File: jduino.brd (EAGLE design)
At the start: 58.1 x 66 mm, 20 parts, among them IC1 L4931, IC2 ATMEGA48/88/168-PU, J1 Analog I/O, J2 Digital I/O, J3 Digital I/O, J5 Power Jumpers, J6 FTDI Jumpers, J7 POWER 6 - 36V, Q1 16 mHz

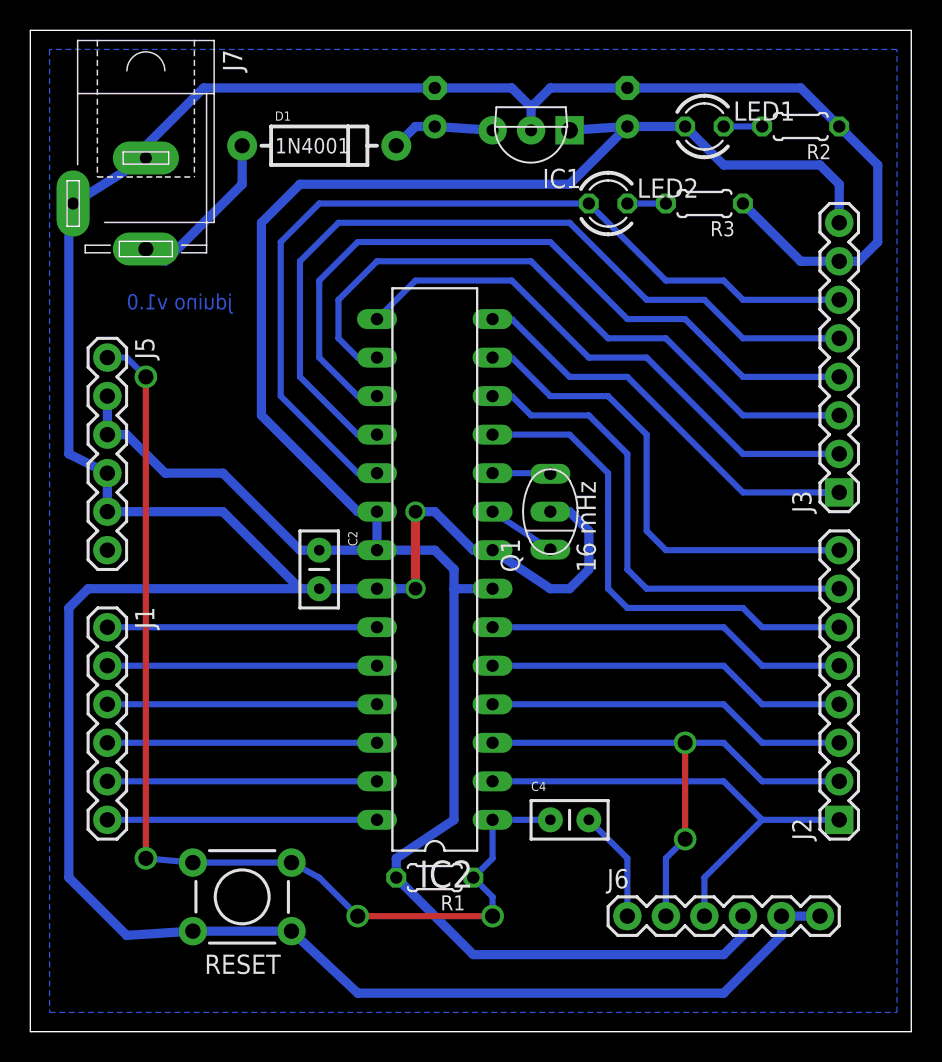
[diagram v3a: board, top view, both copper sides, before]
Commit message: Fixed pad sizes.
Replaced original parts from the Arduino robotics book with components
from the SparkFun libraries so that pads would be properly sized.
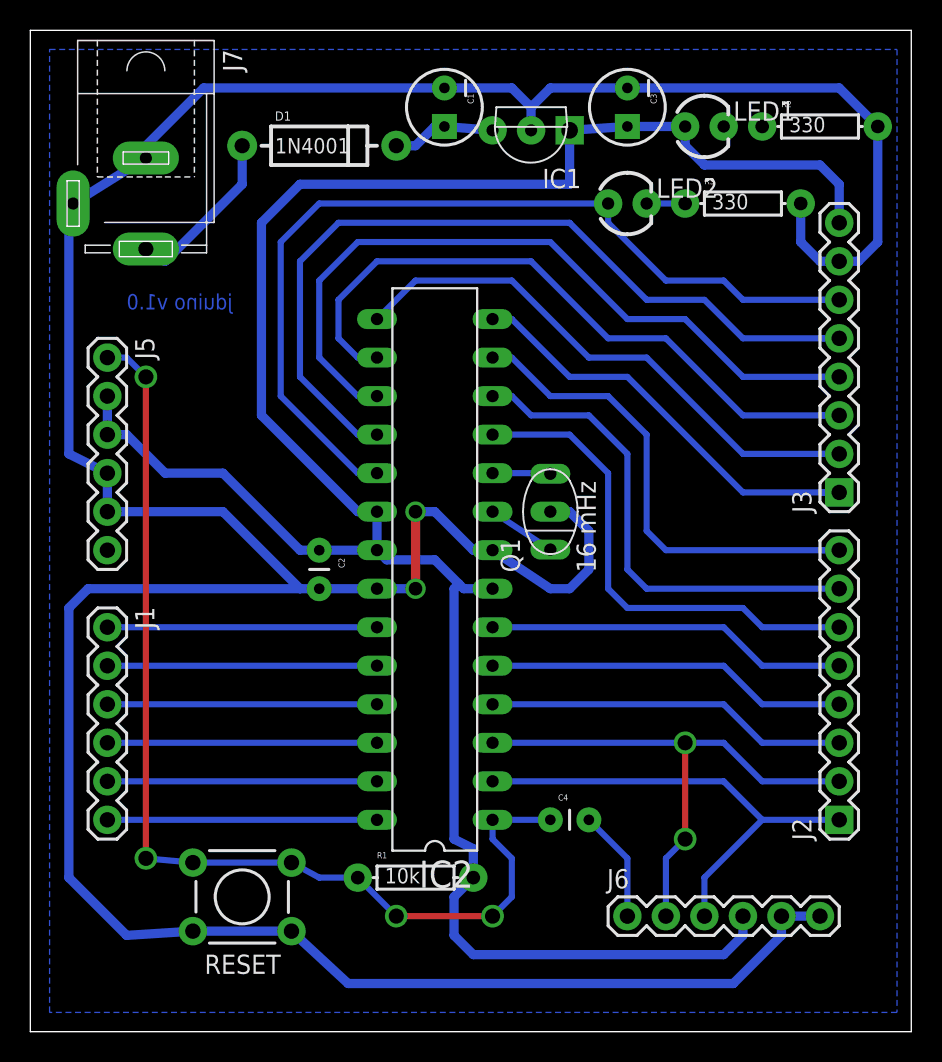
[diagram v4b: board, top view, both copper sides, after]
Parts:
- C1: value 220uf 10v -> 220 uF; device rcl:E2,5-6 -> SparkFun-Capacitors:CPOL-RADIAL-10UF-25V
- C2, C4: value 0.1uF -> 0.1 uF; device SparkFun-Passives:CAP-PTH-SMALL2 -> SparkFun-Capacitors:CAP-PTH-SMALL
- C3: value 220uf 50v -> 220 uF; device rcl:E2,5-6 -> SparkFun-Capacitors:CPOL-RADIAL-10UF-25V
- LED1: value Power LED -> POWER; device led:LED3MM -> SparkFun-LED:LED3MM
- LED2: value LED 13 -> PIN 13; device led:LED3MM -> SparkFun-LED:LED3MM
- R1: value 10K -> 10k; device rcl:0204/5 -> SparkFun-Passives:AXIAL-0.3
- R2, R3: device rcl:0204/5 -> SparkFun-Resistors:AXIAL-0.3
- moved C3 12.7 mm to (39.4, 61.0), flipped to the top, turned to 270 degrees
- moved C1 12.1 mm to (27.3, 61.0), flipped to the top, turned to 270 degrees
- moved R3 2.54 mm to (47.0, 54.6), turned to 0 degrees
- moved R1 1.27 mm to (25.4, 10.2), turned to 0 degrees
- moved R2 1.27 mm to (52.1, 59.7), turned to 0 degrees
- moved LED2 1.27 mm to (39.4, 54.6)
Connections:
- net +5V: now also C3.1, R1.P$2; no longer C1.+, R1.2
- net GND: now also C1.2, C3.2, R2.P$2, R3.P$2; no longer C1.-, C3.-, R2.1, R3.1
- net N$26: now also R2.P$1; no longer R2.2
- net N$4: now also R3.P$1; no longer R3.2
- net N$6: now also C1.1; no longer C3.+
- net RESET: now also R1.P$1; no longer R1.1
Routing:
- net +5V: track 154.9 -> 151.5 mm
- net N$26: track 2.54 -> 0.00 mm
- net GND: track 235.2 -> 233.9 mm
- net D13: track 60.4 -> 61.1 mm
